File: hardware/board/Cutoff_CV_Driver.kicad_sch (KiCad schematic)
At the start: 18 parts

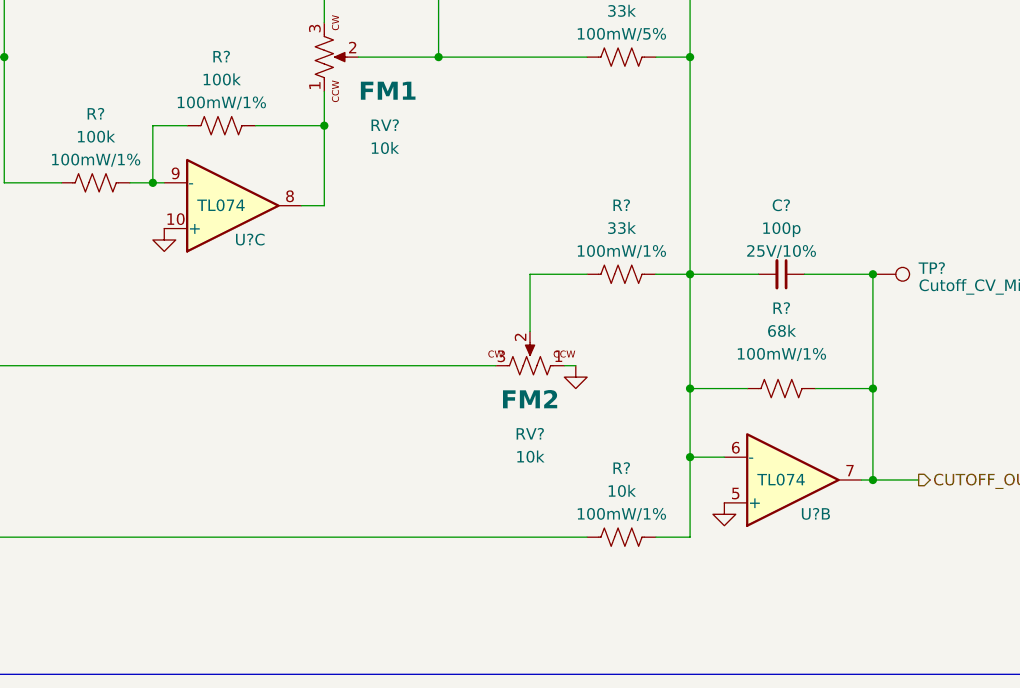
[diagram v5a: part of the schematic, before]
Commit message: First Draft of layout V2 (All components facing the same way)
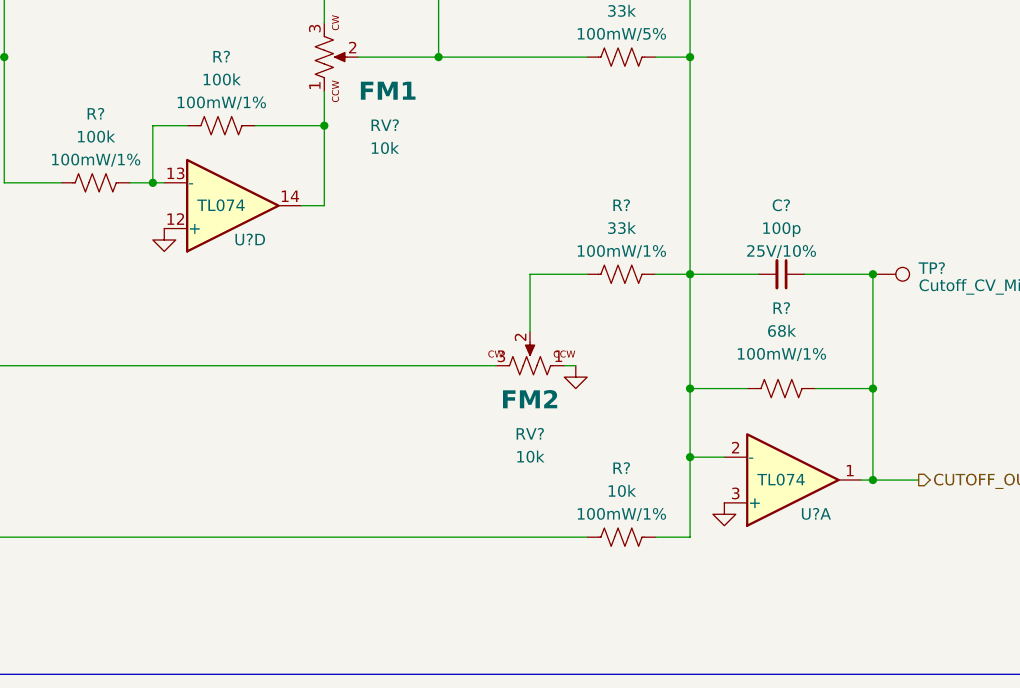
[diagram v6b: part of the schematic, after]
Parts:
- removed U? (x2): TL074, Package_SO:TSSOP-14_4.4x5mm_P0.65mm, symbol winterbloom:TL074
- added U? (x2): TL074, Package_SO:TSSOP-14_4.4x5mm_P0.65mm, symbol winterbloom:TL074
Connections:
- net CUTOFF_OUT: now also U?.1
- net GND: now also U?.12 (+), U?.3 (+)
- net at R?.1, R?.2: now also U?.13 (-)
- net at C?.2, R?.1, R?.1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: now also U?.2 (-)
- net at R?.1, RV?.1: now also U?.14

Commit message: Rough Draft of Routing Complete. Ugly but Passes DRC
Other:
- note added: "Mixes the various modulation sources for the Cutoff Frequency CV input: 5v Nominal Max CV Cutoff: ~15khz"
- note removed: "Mixes the various modulation sources for the Cutoff Frequency CV input: 5v Nominal Max CV Cutoff: ~15khz LED Max Brightness: 3.3mA"
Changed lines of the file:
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@@
     (fill (type none))
   )
-  (text "Mixes the various modulation sources for the Cutoff Frequency\n\nCV input: 5v Nominal Max\n\nCV Cutoff: ~15khz\n\nLED Max Brightness: 3.3mA\n\n"
-    (at 21.59 44.45 0)
+  (text "Mixes the various modulation sources for the Cutoff Frequency\n\nCV input: 5v Nominal Max\n\nCV Cutoff: ~15khz\n\n"
+    (at 22.225 40.005 0)
     (effects (font (size 1.27 1.27)) (justify left bottom))
   )

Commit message: hardware: minor fixes and aesthetic updates
- Fix HP LEDs being backwards
- Switch power header, pot, and jack footprints to longpad variants
- Make the text size on the front side larger
- Add "red" and "blue" text next to respective LEDs on front side
- Adjusted zone thermal spoke for better connection to GND pads
- Squished the solder jumpers for instability type closer together
- Minor adjustments to traces to accommodate longpad footprints
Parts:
- J? (x2): footprint winterbloom:AudioJack_WQP518MA_Compact_S -> winterbloom:AudioJack_WQP518MA_Compact_S_LongPads
- RV? (x3): footprint winterbloom:Potentiometer_Alpha_R0904N -> winterbloom:Potentiometer_Alpha_R0904N_LongPads
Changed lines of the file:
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@@
       (effects (font (size 1.27 1.27)))
     )
-    (property "Footprint" "winterbloom:Potentiometer_Alpha_R0904N" (at 96.52 71.12 0)
+    (property "Footprint" "winterbloom:Potentiometer_Alpha_R0904N_LongPads" (at 96.52 71.12 0)
       (effects (font (size 1.27 1.27)) hide)
     )
@@
       (effects (font (size 1.27 1.27)))
     )
-    (property "Footprint" "winterbloom:AudioJack_WQP518MA_Compact_S" (at 95.25 91.44 0)
+    (property "Footprint" "winterbloom:AudioJack_WQP518MA_Compact_S_LongPads" (at 95.25 91.44 0)
       (effects (font (size 1.27 1.27)) hide)
     )
@@
       (effects (font (size 1.27 1.27)))
     )
-    (property "Footprint" "winterbloom:Potentiometer_Alpha_R0904N" (at 167.64 121.92 0)
+    (property "Footprint" "winterbloom:Potentiometer_Alpha_R0904N_LongPads" (at 167.64 121.92 0)
       (effects (font (size 1.27 1.27)) hide)
     )
@@
       (effects (font (size 1.27 1.27)))
     )
-    (property "Footprint" "winterbloom:AudioJack_WQP518MA_Compact_S" (at 95.25 125.73 0)
+    (property "Footprint" "winterbloom:AudioJack_WQP518MA_Compact_S_LongPads" (at 95.25 125.73 0)
       (effects (font (size 1.27 1.27)) hide)
     )
@@
       (effects (font (size 1.27 1.27)) (justify right))
     )
-    (property "Footprint" "winterbloom:Potentiometer_Alpha_R0904N" (at 156.21 99.06 0)
-      (effects (font (size 1.27 1.27)) hide)
-    )
+    (property "Footprint" "winterbloom:Potentiometer_Alpha_R0904N_LongPads" (at 156.21 99.06 0)
+      (effects (font (size 1.27 1.27)) hide)
+    )
